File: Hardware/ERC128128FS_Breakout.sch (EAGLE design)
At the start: 19 parts, among them J1 ER-CON2.0-2P-SMD, J3 ER-CON31HT-1, U1 PMV160UP,215

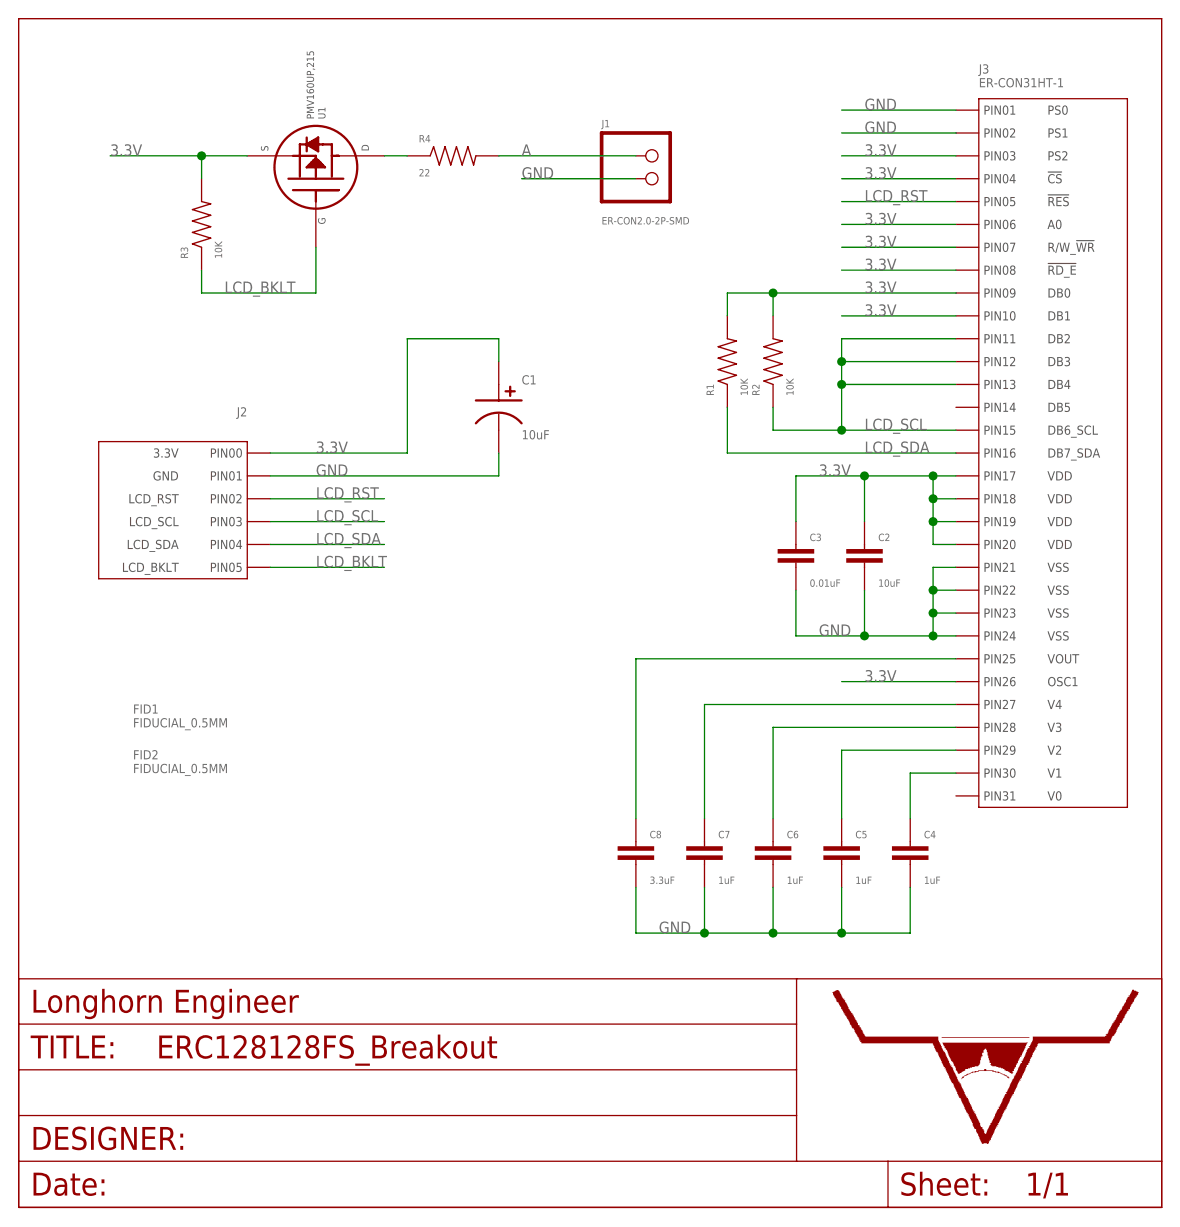
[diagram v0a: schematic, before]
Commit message: Updated to new library style.
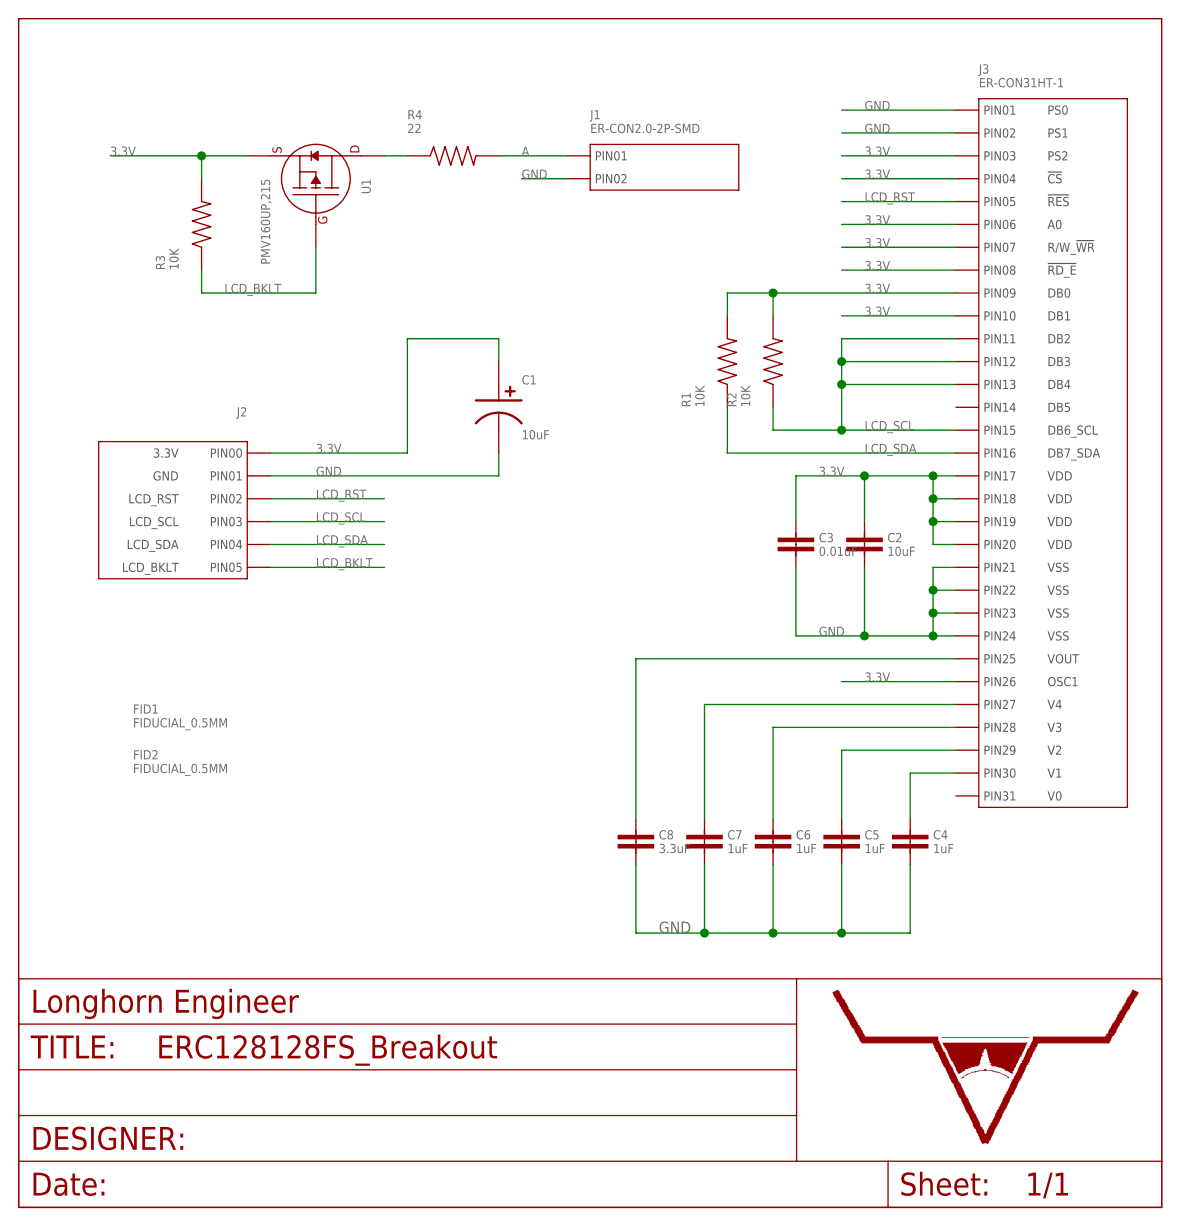
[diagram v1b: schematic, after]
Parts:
- C2: device PP_Passives:CAPACITOR_NON_POLAR1206 -> PP_Passives:CAPACITOR_NON_POLAR_1206
- C3, C4, C5, C6, C7, C8: device PP_Passives:CAPACITOR_NON_POLAR0603 -> PP_Passives:CAPACITOR_NON_POLAR_0603
- J1: device PP_Connectors:PH_1X02ER-CON2.0-2P-SMD -> PP_Connectors:CON_01X02_ER-CON2.0-2P-SMD
- J3: device PP_Connectors:ER-CON31HT-1 -> PP_Connectors:CON_01X31_ER-CON31HT-1
- R1, R2, R3, R4: device PP_Passives:RESISTOR0603 -> PP_Passives:RESISTOR_0603
- U1: device PP_DiscreteSemi:MOSFET_P-CHANNEL_SINGLESOT-23 -> PP_DiscreteSemi:MOSFET_P-CHANNEL_SINGLE_SOT-23
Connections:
- net A: now also J1.PIN1; no longer J1.1
- net GND: now also J1.PIN2; no longer J1.2
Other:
- moved on the sheet: C2, C3, C4, C5, C6, C7, C8, J1

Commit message: Basic Library complete.
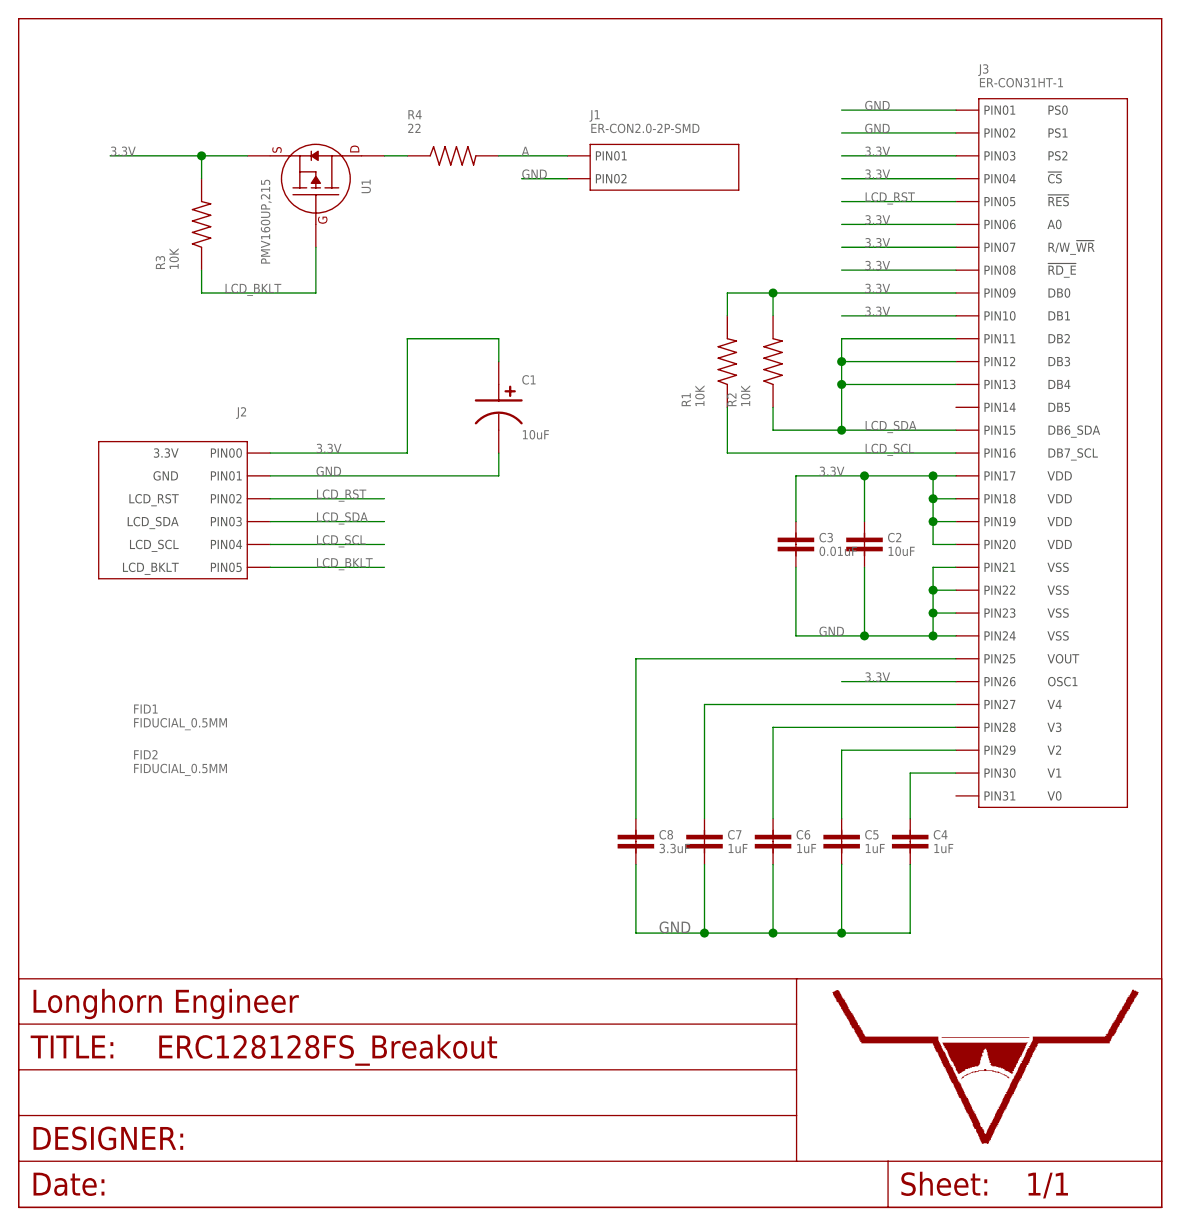
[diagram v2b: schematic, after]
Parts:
- J2: LABEL03 LCD_SCL -> LCD_SDA; LABEL04 LCD_SDA -> LCD_SCL
- J3: LABEL15 DB6_SCL -> DB6_SDA; LABEL16 DB7_SDA -> DB7_SCL
- U$1: REVNUM REV: 1 -> REV: 2
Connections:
- net LCD_SCL: now also J2.PIN4, J3.PIN16, R1.1; no longer J2.PIN3, J3.PIN11, J3.PIN12, J3.PIN13, J3.PIN15, R2.1
- net LCD_SDA: now also J2.PIN3, J3.PIN11, J3.PIN12, J3.PIN13, J3.PIN15, R2.1; no longer J2.PIN4, J3.PIN16, R1.1
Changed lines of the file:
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@@
 <?xml version="1.0" encoding="utf-8"?>
 <!DOCTYPE eagle SYSTEM "eagle.dtd">
-<eagle version="6.6.0">
+<eagle version="7.4.0">
 <drawing>
 <settings>
@@
 <attribute name="LABEL13" value="DB4"/>
 <attribute name="LABEL14" value="DB5"/>
-<attribute name="LABEL15" value="DB6_SCL"/>
-<attribute name="LABEL16" value="DB7_SDA"/>
+<attribute name="LABEL15" value="DB6_SDA"/>
+<attribute name="LABEL16" value="DB7_SCL"/>
 <attribute name="LABEL17" value="VDD"/>
 <attribute name="LABEL18" value="VDD"/>
@@
 <attribute name="LABEL01" value="GND"/>
 <attribute name="LABEL02" value="LCD_RST"/>
-<attribute name="LABEL03" value="LCD_SCL"/>
-<attribute name="LABEL04" value="LCD_SDA"/>
+<attribute name="LABEL03" value="LCD_SDA"/>
+<attribute name="LABEL04" value="LCD_SCL"/>
 <attribute name="LABEL05" value="LCD_BKLT"/>
 </part>
@@
 <part name="U$1" library="PP_Aesthetics" deviceset="LHE_FRAME" device="">
 <attribute name="DNAME" value="Parker Dillmann"/>
-<attribute name="REVNUM" value="REV: 1"/>
+<attribute name="REVNUM" value="REV: 2"/>
 </part>
 <part name="FID1" library="MF_Aesthetics" deviceset="FIDUCIAL" device="_0.5MM"/>
@@
 <net name="LCD_SCL" class="0">
 <segment>
+<pinref part="J3" gate="G$1" pin="PIN16"/>
+<wire x1="-22.86" y1="83.82" x2="-48.26" y2="83.82" width="0.1524" layer="91"/>
+<label x="-33.02" y="83.82" size="1.016" layer="95" font="vector"/>
+<pinref part="R1" gate="G$1" pin="1"/>
+<wire x1="-48.26" y1="83.82" x2="-48.26" y2="88.9" width="0.1524" layer="91"/>
+</segment>
+<segment>
+<pinref part="J2" gate="G$1" pin="PIN4"/>
+<wire x1="-86.36" y1="73.66" x2="-99.06" y2="73.66" width="0.1524" layer="91"/>
+<label x="-93.98" y="73.66" size="1.016" layer="95" font="vector"/>
+</segment>
+</net>
+<net name="LCD_SDA" class="0">
+<segment>
 <pinref part="J3" gate="G$1" pin="PIN15"/>
 <wire x1="-22.86" y1="86.36" x2="-35.56" y2="86.36" width="0.1524" layer="91"/>
@@
 </segment>
 </net>
-<net name="LCD_SDA" class="0">
-<segment>
-<pinref part="J3" gate="G$1" pin="PIN16"/>
-<wire x1="-22.86" y1="83.82" x2="-48.26" y2="83.82" width="0.1524" layer="91"/>
-<label x="-33.02" y="83.82" size="1.016" layer="95" font="vector"/>
-<pinref part="R1" gate="G$1" pin="1"/>
-<wire x1="-48.26" y1="83.82" x2="-48.26" y2="88.9" width="0.1524" layer="91"/>
-</segment>
-<segment>
-<pinref part="J2" gate="G$1" pin="PIN4"/>
-<wire x1="-86.36" y1="73.66" x2="-99.06" y2="73.66" width="0.1524" layer="91"/>
-<label x="-93.98" y="73.66" size="1.016" layer="95" font="vector"/>
-</segment>
-</net>
